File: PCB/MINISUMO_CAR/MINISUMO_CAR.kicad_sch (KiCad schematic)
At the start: 12 parts, among them U1 XY-XHB2.54-4A11, U2 XY-XHB2.54-4A11, U3 XY-XHB2.54-4A11, U4 XY-XHB2.54-4A11, U5 XY-XHB2.54-3A11, U6 XY-XHB2.54-3A11

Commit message: add push init and driver H
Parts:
- added C1: 100nf, symbol Device:C
- added GND1: PH_GND, Connector_PinHeader_2.00mm:PinHeader_1x01_P2.00mm_Vertical, symbol Connector:TestPoint
- added INA1: INA1, Connector_PinHeader_2.00mm:PinHeader_1x01_P2.00mm_Vertical, symbol Connector:TestPoint
- added INA2: INA2, Connector_PinHeader_2.00mm:PinHeader_1x01_P2.00mm_Vertical, symbol Connector:TestPoint
- added INB1: INB1, Connector_PinHeader_2.00mm:PinHeader_1x01_P2.00mm_Vertical, symbol Connector:TestPoint
- added INB2: INB2, Connector_PinHeader_2.00mm:PinHeader_1x01_P2.00mm_Vertical, symbol Connector:TestPoint
- added PWM1, PWM2: PWM, Connector_PinHeader_2.00mm:PinHeader_1x01_P2.00mm_Vertical, symbol Connector:TestPoint
- added R1: 10k, symbol Device:R
- added SW1: SW_Push, symbol Switch:SW_Push
- added VCC1: M_VCC, Connector_PinHeader_2.00mm:PinHeader_1x01_P2.00mm_Vertical, symbol Connector:TestPoint
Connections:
- net +BATT: now also VCC1.1
- net -BATT: now also C1.2, GND1.1, SW1.2
- net 3+: now also R1.1
- new net: C1.1, R1.2, SW1.1
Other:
- note added: "Linea GND puente H"
- note added: "Linea VCC puente H"
- note added: "PUENTE H"
- note added: "PUENTE H INA1"
- note added: "PUENTE H INA2"
- note added: "PUENTE H INB1"
- note added: "PUENTE H INB2"
- note added: "PWM del MOTOR1"
- note added: "PWM del MOTOR2"
- note added: "Push init"

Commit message: Finish to day 7_27_2026
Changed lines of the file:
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@@
+	)
+	(rectangle
+		(start 142.24 16.51)
+		(end 177.8 21.59)
+		(stroke
+			(width 0)
+			(type default)
+		)
+		(fill
+			(type none)
+		)
 	)
 	(rectangle
@@
 	)
 	(rectangle
+		(start 142.24 16.51)
+		(end 177.8 44.45)
+		(stroke
+			(width 0)
+			(type default)
+		)
+		(fill
+			(type none)
+		)
+	)
+	(rectangle
 		(start 68.58 44.45)
 		(end 142.24 102.87)
@@
 	(text "Push init"
 		(exclude_from_sim no)
-		(at 164.592 19.05 0)
-		(effects
-			(font
+		(at 161.036 19.304 0)
+		(effects
+			(font

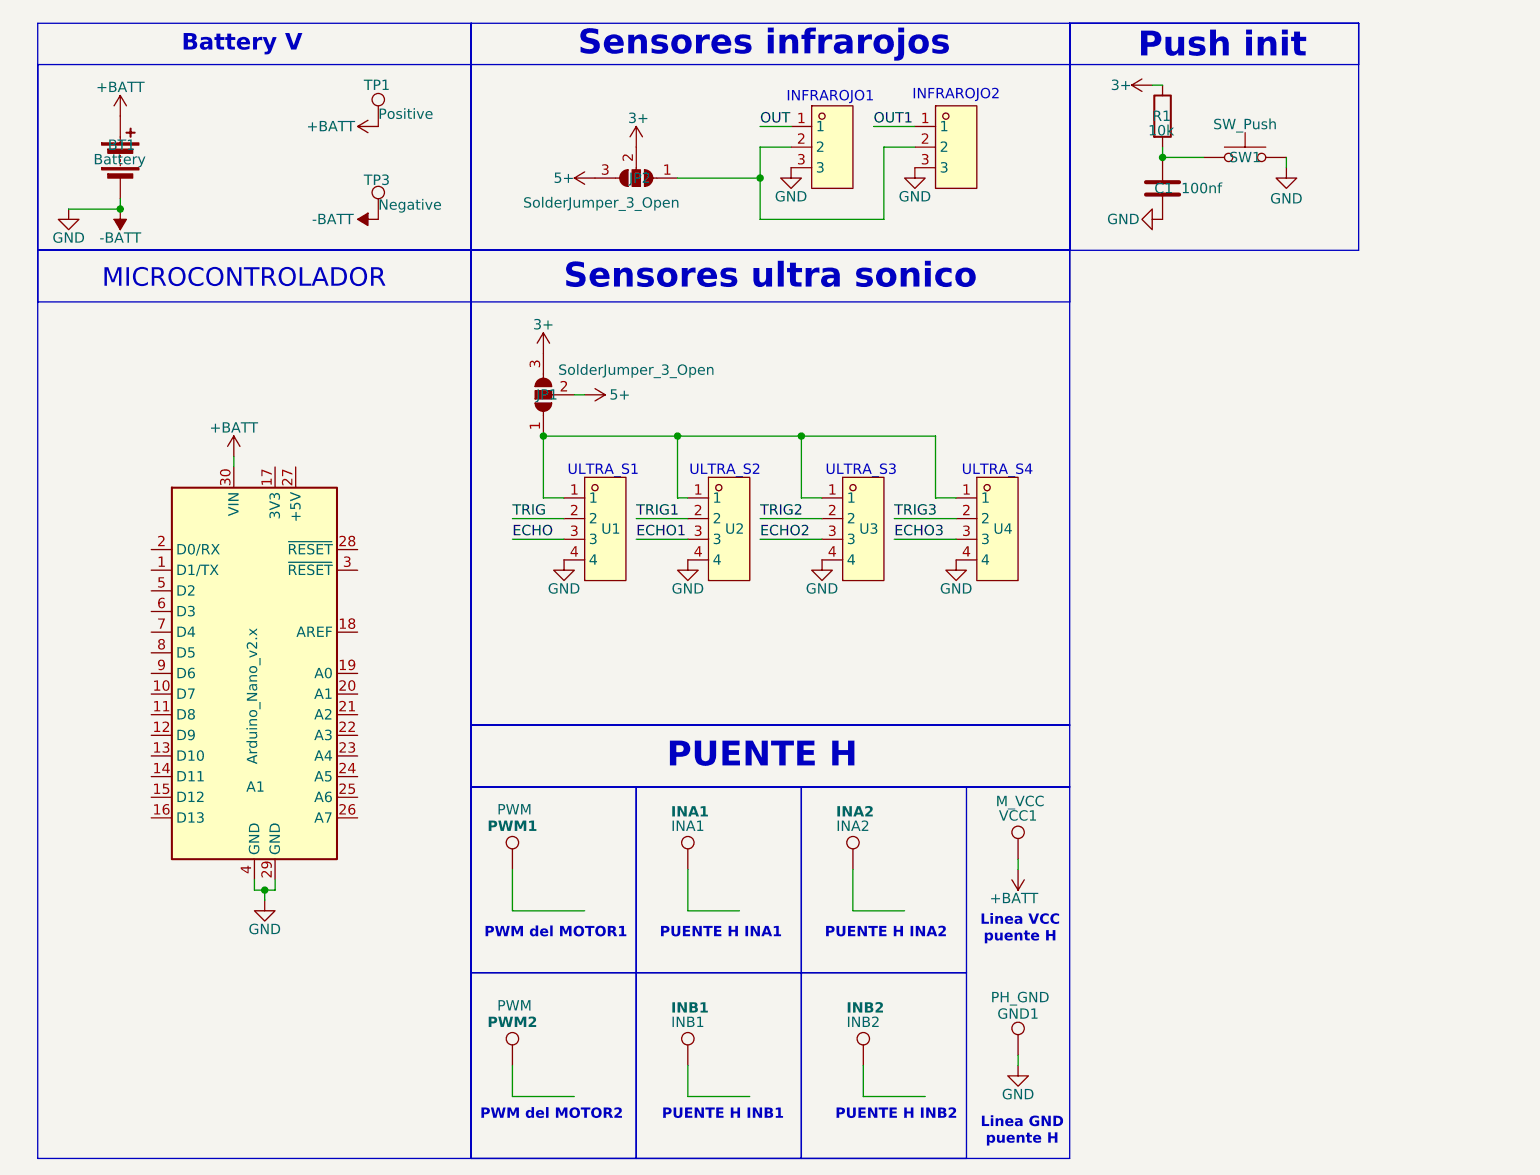
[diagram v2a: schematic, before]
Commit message: update pin out of sensors
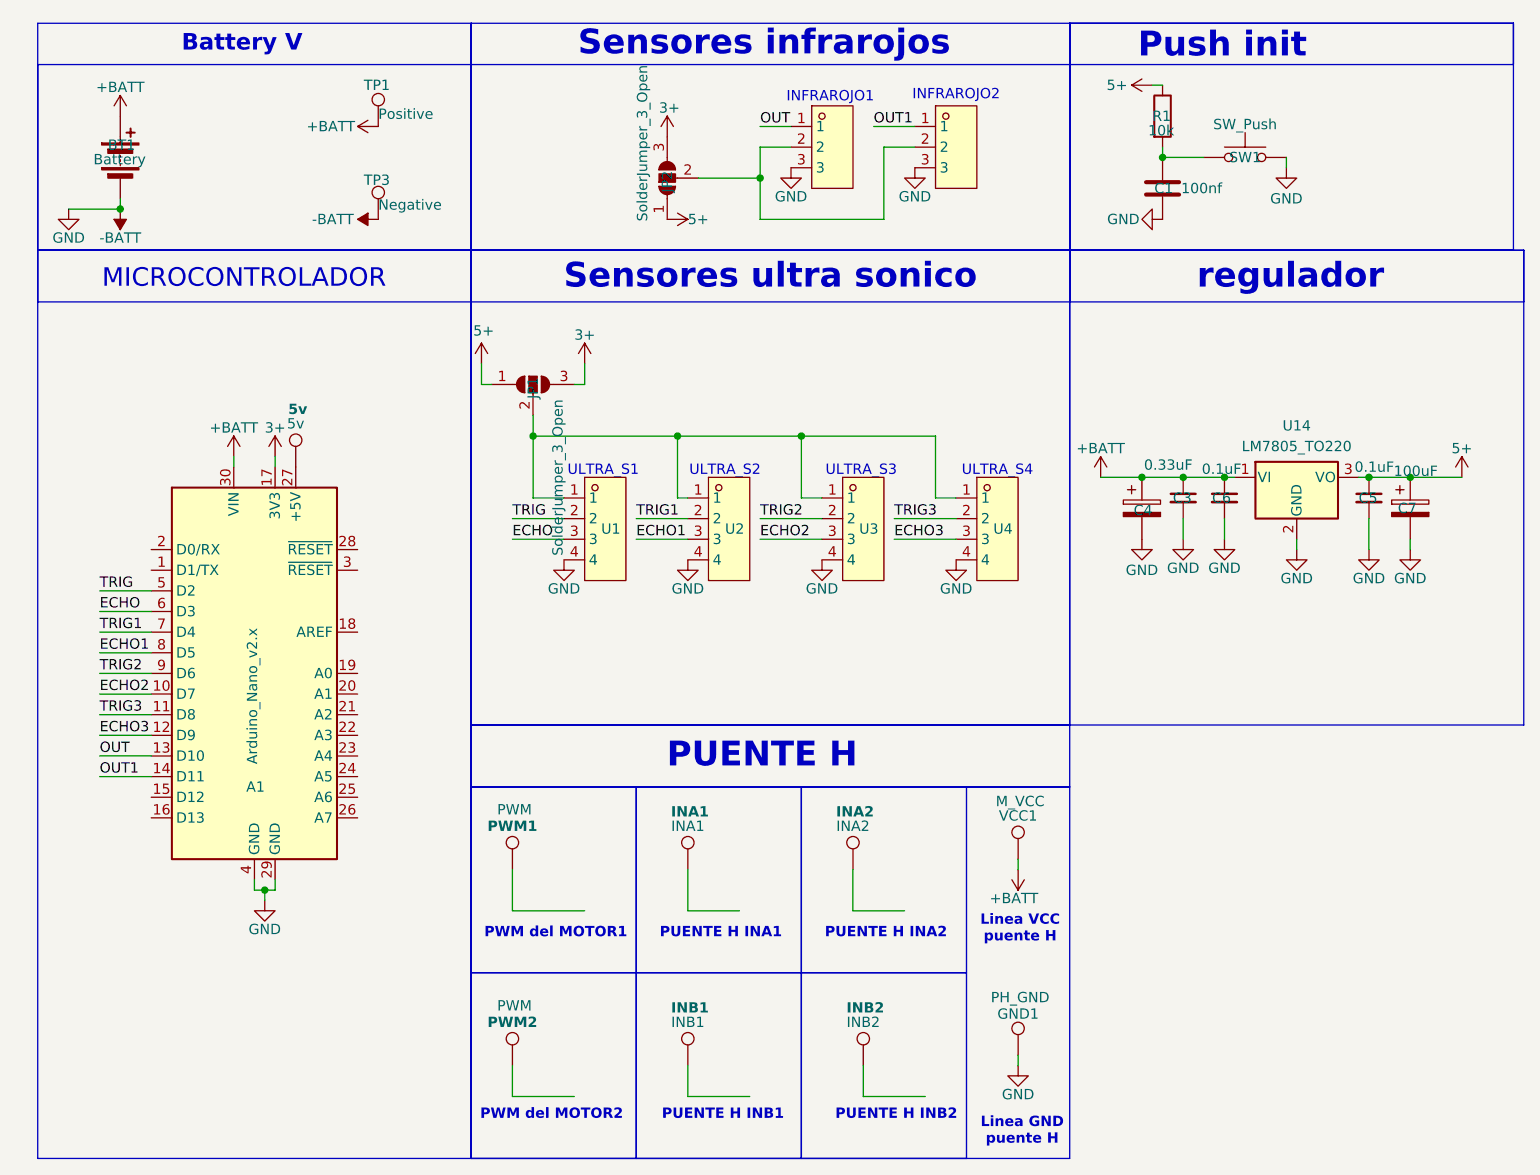
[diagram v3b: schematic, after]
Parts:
- added 5v: 5v, Connector_PinHeader_2.00mm:PinHeader_1x01_P2.00mm_Vertical, symbol Connector:TestPoint
- added C3: 0.33uF, Capacitor_SMD:C_0805_2012Metric, symbol Device:C_Small
- added C4: 470uf, Capacitor_SMD:CP_Elec_10x10.5, symbol Device:C_Polarized
- added C5, C6: 0.1uF, Capacitor_SMD:C_0805_2012Metric, symbol Device:C_Small
- added C7: 100uF, Capacitor_SMD:CP_Elec_6.3x7.7, symbol Device:C_Polarized
- added U14: LM7805_TO220, Package_TO_SOT_THT:TO-220-3_Vertical, symbol Regulator_Linear:LM7805_TO220
- R1: footprint (none) -> Resistor_THT:R_Axial_DIN0411_L9.9mm_D3.6mm_P15.24mm_Horizontal
- SW1: footprint (none) -> Button_Switch_THT:SW_PUSH_6mm_H5mm
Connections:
- net +BATT: now also C3.1, C4.1, C6.1, U14.1 (VI)
- net -BATT: now also C3.2, C4.2, C5.2, C6.2, C7.2, U14.2 (GND)
- net 3+: now also A1.17 (3V3), JP2.3 (B); no longer JP2.2 (C), R1.1
- net 5+: now also JP1.1 (A), JP2.1 (A), R1.1, C5.1, C7.1, U14.3 (VO); no longer JP1.2 (C), JP2.3 (B)
- net ECHO: now also A1.6 (D3)
- net ECHO1: now also A1.8 (D5)
- net ECHO2: now also A1.10 (D7)
- net ECHO3: now also A1.12 (D9)
- net OUT: now also A1.13 (D10)
- net OUT1: now also A1.14 (D11)
- net TRIG: now also A1.5 (D2)
- net TRIG1: now also A1.7 (D4)
- net TRIG2: now also A1.9 (D6)
- net TRIG3: now also A1.11 (D8)
- net at U1.1, U2.1, U3.1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: now also JP1.2 (C); no longer JP1.1 (A)
- net at U5.2, U6.2: now also JP2.2 (C); no longer JP2.1 (A)
- net at A1.27 (+5V): now also 5v.1
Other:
- note added: "regulador"
- moved on the sheet: JP1, JP2

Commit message: update pin of sensor v2
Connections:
- net OUT: now also A1.15 (D12); no longer A1.13 (D10)
- net OUT1: now also A1.16 (D13); no longer A1.14 (D11)
- net D11: now reaches PWM2.1
- net D11: now also A1.14 (D11)
- net A2: now reaches INB1.1
- net A2: now also A1.21 (A2)
- net A0: now reaches A1.19 (A0)
- net A0: now also INA1.1
- net A1: now reaches A1.20 (A1)
- net A1: now also INA2.1
- net A3: now reaches A1.22 (A3)
- net A3: now also INB2.1
- net A4: now reaches A1.23 (A4)
- net A4: now also C1.1, R1.2, SW1.1
- net A5: now reaches A1.24 (A5)
- net A6: now reaches A1.25 (A6)
- net A7: now reaches A1.26 (A7)
- net D10: now reaches PWM1.1
- net D10: now also A1.13 (D10)

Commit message: update of sensor v3
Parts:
- removed JP1, JP2: SolderJumper_3_Open, symbol Jumper:SolderJumper_3_Open
- added GND2: PH_GND, Connector_PinHeader_2.00mm:PinHeader_1x01_P2.00mm_Vertical, symbol Connector:TestPoint
- added pin_libre1: pin_libre, Connector_PinHeader_2.00mm:PinHeader_1x01_P2.00mm_Vertical, symbol Connector:TestPoint
- C1: footprint (none) -> Capacitor_SMD:C_0805_2012Metric
- R1: footprint Resistor_THT:R_Axial_DIN0411_L9.9mm_D3.6mm_P15.24mm_Horizontal -> Resistor_SMD:R_0805_2012Metric_Pad1.20x1.40mm_HandSolder
- renumbered 5v to 5v1
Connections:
- net -BATT: now also GND2.1
- net 5+: now also U1.1, U2.1, U3.1, U4.1, U5.2, U6.2
- net A5: now also pin_libre1.1
- net ECHO: now also A1.5 (D2); no longer A1.6 (D3)
- net ECHO1: now also A1.7 (D4); no longer A1.8 (D5)
- net ECHO3: now also A1.11 (D8); no longer A1.12 (D9)
- net TRIG: now also A1.6 (D3); no longer A1.5 (D2)
- net TRIG1: now also A1.8 (D5); no longer A1.7 (D4)
- net TRIG3: now also A1.12 (D9); no longer A1.11 (D8)
- net A6: no longer names the net of A1.25 (A6)
- net A7: no longer names the net of A1.26 (A7)
- no-connect marks 0 -> 7
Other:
- moved on the sheet: 5v1
